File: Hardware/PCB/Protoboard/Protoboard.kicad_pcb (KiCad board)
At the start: 2 copper layers, 17 parts, among them J1 Conn_01x05_Female, J2 Conn_01x08_Female, J3 Conn_01x08_Female, U1 MAX6971ANG_

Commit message: Finished Protoboard
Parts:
- added H1: MountingHole, MountingHole:MountingHole_2.2mm_M2, F.Cu at (119.4, 68.6)
- added H2: MountingHole, MountingHole:MountingHole_2.2mm_M2, F.Cu at (152.4, 68.6)
- added H3: MountingHole, MountingHole:MountingHole_2.2mm_M2, F.Cu at (152.4, 104.1)
- added H4: MountingHole, MountingHole:MountingHole_2.2mm_M2, F.Cu at (119.4, 104.1)
- moved R5 4.68 mm to (128.3, 82.0), turned to 90 degrees
- moved R7 4.68 mm to (128.3, 87.1), turned to 90 degrees
- moved R11 4.68 mm to (128.3, 97.3), turned to 90 degrees
- moved R9 4.68 mm to (128.3, 92.2), turned to 90 degrees
- moved J1 3.25 mm to (124.7, 68.4)
- moved R10 1.44 mm to (131.8, 94.7), turned to 90 degrees
- moved R12 1.44 mm to (131.8, 99.8), turned to 90 degrees
- moved R8 1.44 mm to (131.8, 89.7), turned to 90 degrees
- moved R6 1.44 mm to (131.8, 84.6), turned to 90 degrees
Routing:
- net Net-(J3-Pad7): track 0.00 -> 16.1 mm
- net Net-(J3-Pad3): track 0.00 -> 16.1 mm
- net Net-(J3-Pad5): track 0.00 -> 16.1 mm
- net Net-(J3-Pad6): track 0.00 -> 16.1 mm
- net Net-(J3-Pad8): track 0.00 -> 16.1 mm
- net Net-(J3-Pad4): track 0.00 -> 16.1 mm
- net Net-(J3-Pad2): track 0.00 -> 16.1 mm
- net Net-(J3-Pad1): track 0.00 -> 15.3 mm
- net Net-(J1-Pad4): track 0.00 -> 8.14 mm
- net Net-(J1-Pad2): track 0.00 -> 8.14 mm
- net Net-(J1-Pad3): track 0.00 -> 8.14 mm
- net Net-(J2-Pad8): track 0.00 -> 4.93 mm
- net Net-(J2-Pad7): track 0.00 -> 4.93 mm
- net Net-(J2-Pad6): track 0.00 -> 4.93 mm
- net Net-(J2-Pad5): track 0.00 -> 4.93 mm
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- added copper zone on B.Cu, net GND
- added copper zone on F.Cu, net VCC
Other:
- board outline added: 39.1 x 41.7 mm

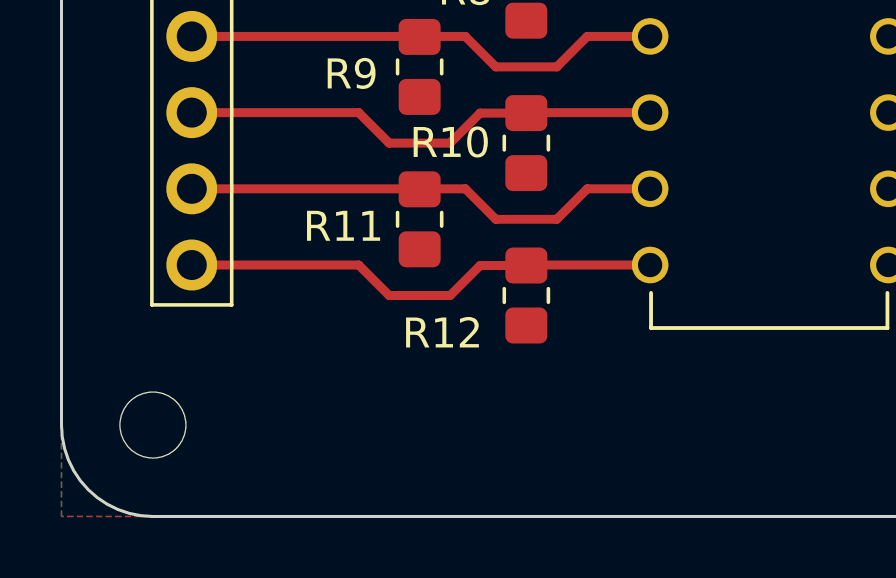
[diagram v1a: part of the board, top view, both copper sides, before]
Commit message: Fixed Silkscreen
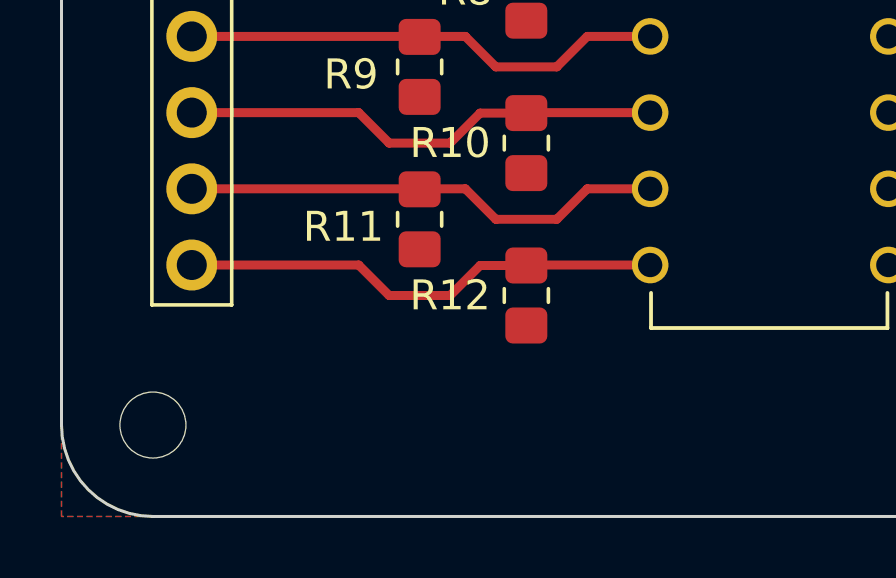
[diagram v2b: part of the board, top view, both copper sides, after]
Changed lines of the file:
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@@
     (property "Sheetname" "")
     (attr smd)
-    (fp_text reference "R12" (at -1.27 -2.794 180) (layer "F.SilkS")
+    (fp_text reference "R12" (at 0 -2.54 180) (layer "F.SilkS")
       (effects (font (size 1 1) (thickness 0.15)))
     )

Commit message: Finished
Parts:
- renumbered R3 to R1, R1 to R3
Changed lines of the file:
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@@
     (property "Sheetname" "")
     (attr smd)
-    (fp_text reference "R1" (at -3.048 0) (layer "F.SilkS")
+    (fp_text reference "R3" (at -3.048 0) (layer "F.SilkS")
       (effects (font (size 1 1) (thickness 0.15)))
     )
@@
     (property "Sheetname" "")
     (attr smd)
-    (fp_text reference "R3" (at -3.048 0) (layer "F.SilkS")
+    (fp_text reference "R1" (at -3.048 0) (layer "F.SilkS")
       (effects (font (size 1 1) (thickness 0.15)))
     )
